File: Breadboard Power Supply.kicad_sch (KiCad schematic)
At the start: 33 parts, among them J1 USB-C Power Only, J10 Conn_01x02_Male, J11 Conn_01x02_Male, J2 Conn_01x02_Male, J3 Conn_01x02_Male, J4 Conn_01x02_Male, J5 Conn_01x02_Male, J6 Conn_01x02_Male, J7 Conn_01x02_Male, J8 Conn_01x02_Male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

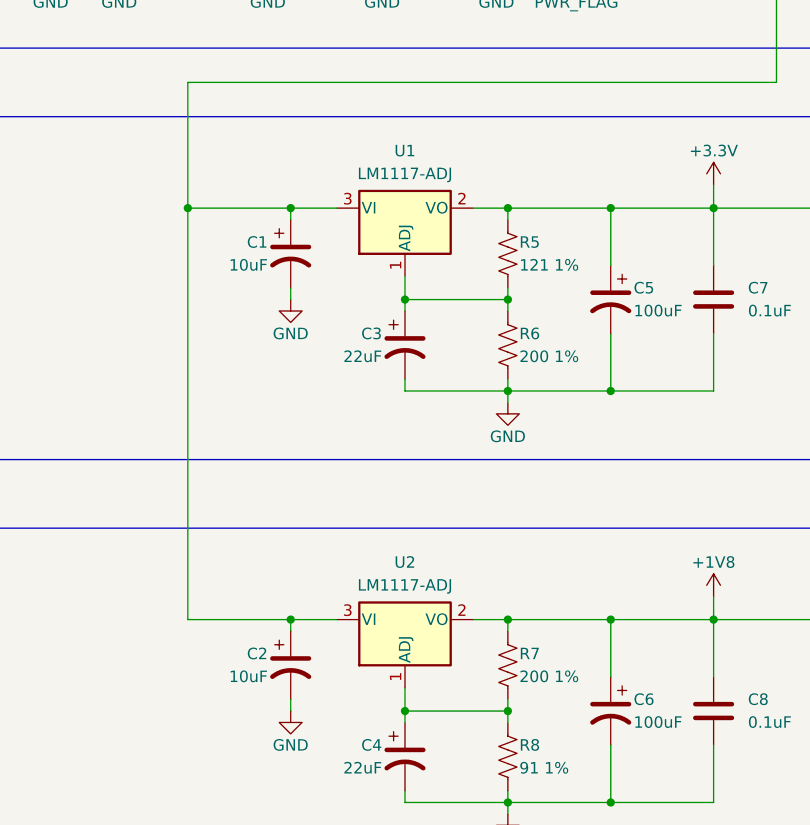
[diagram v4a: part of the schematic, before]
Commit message: Changed LM1117 symbol.
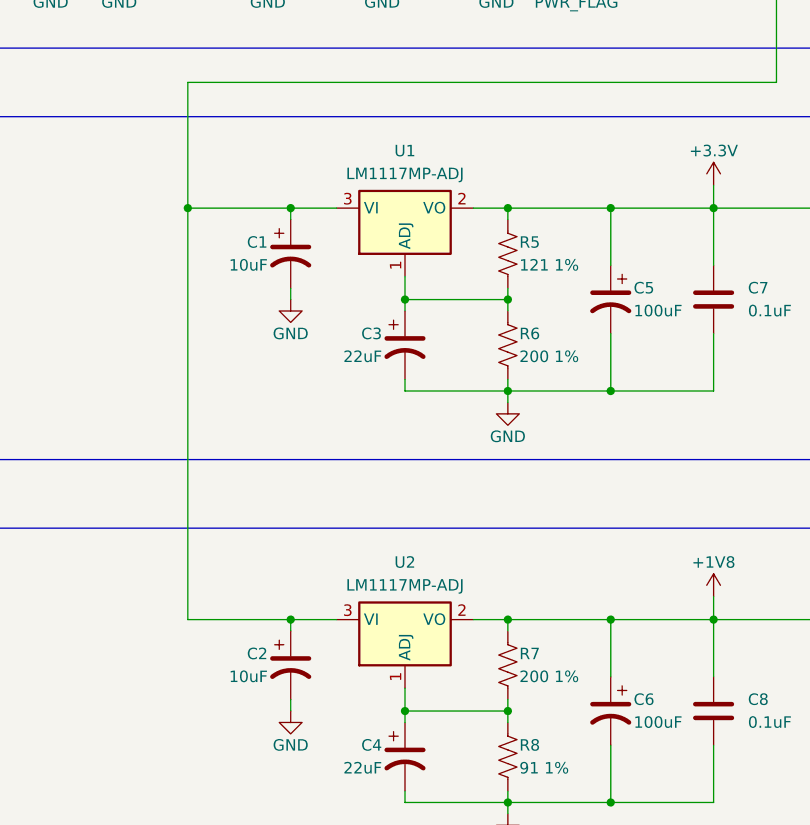
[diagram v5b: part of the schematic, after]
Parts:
- removed U1, U2: LM1117-ADJ, My Breadboard Power Supply Libraries:VREG_LM1117MPX-3.3_NOPB, symbol Regulator_Linear:LM1117-ADJ
- added U1, U2: LM1117MP-ADJ, Package_TO_SOT_SMD:SOT-223-3_TabPin2, symbol Regulator_Linear:LM1117MP-ADJ
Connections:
- net +1V8: now also U2.2 (VO)
- net +3.3V: now also U1.2 (VO)
- net +5V: now also U1.3 (VI), U2.3 (VI)
- net at C4.1, R7.2, R8.1: now also U2.1 (ADJ)
- net at C3.1, R5.2, R6.1: now also U1.1 (ADJ)
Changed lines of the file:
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@@
-    )
-  )
-  (symbol (lib_id "Regulator_Linear:LM1117-ADJ") (at 105.41 97.79 0) (unit 1)
-    (in_bom yes) (on_board yes) (dnp no)
-    (property "Reference" "U1" (at 105.41 91.44 0)
-      (effects (font (size 1.27 1.27)))
-    )
-    (property "Value" "LM1117-ADJ" (at 105.41 93.98 0)
-      (effects (font (size 1.27 1.27)))
-    )
-    (property "Footprint" "My Breadboard Power Supply Libraries:VREG_LM1117MPX-3.3_NOPB" (at 105.41 97.79 0)
-      (effects (font (size 1.27 1.27)) hide)
-    )
-    (property "Datasheet" "http://www.ti.com/lit/ds/symlink/lm1117.pdf" (at 105.41 97.79 0)
-      (effects (font (size 1.27 1.27)) hide)
-    )
-    (pin "1")
-    (pin "2")
-    (pin "3")
-    (instances
-      (project "Breadboard Power Supply"
-        (path "/a474ae98-d5ea-4288-b242-cd0417157b2d"
-          (reference "U1") (unit 1)
-        )
-      )
     )
   )
@@
     )
   )
-  (symbol (lib_id "Regulator_Linear:LM1117-ADJ") (at 105.41 143.51 0) (unit 1)
-    (in_bom yes) (on_board yes) (dnp no)
-    (property "Reference" "U2" (at 105.41 137.16 0)
-      (effects (font (size 1.27 1.27)))
-    )
-    (property "Value" "LM1117-ADJ" (at 105.41 139.7 0)
-      (effects (font (size 1.27 1.27)))
-    )
-    (property "Footprint" "My Breadboard Power Supply Libraries:VREG_LM1117MPX-3.3_NOPB" (at 105.41 143.51 0)
-      (effects (font (size 1.27 1.27)) hide)
-    )
-    (property "Datasheet" "http://www.ti.com/lit/ds/symlink/lm1117.pdf" (at 105.41 143.51 0)
+  (symbol (lib_id "power:GND") (at 210.82 124.46 0) (unit 1)
+    (in_bom yes) (on_board yes) (dnp no)
+    (property "Reference" "#PWR0115" (at 210.82 130.81 0)
+      (effects (font (size 1.27 1.27)) hide)
+    )
+    (property "Value" "GND" (at 210.82 128.27 0)
+      (effects (font (size 1.27 1.27)))
+    )
+    (property "Footprint" "" (at 210.82 124.46 0)
+      (effects (font (size 1.27 1.27)) hide)
+    )
+    (property "Datasheet" "" (at 210.82 124.46 0)
+      (effects (font (size 1.27 1.27)) hide)
+    )
+    (pin "1")
+    (instances
+      (project "Breadboard Power Supply"
+        (path "/a474ae98-d5ea-4288-b242-cd0417157b2d"
+          (reference "#PWR0115") (unit 1)
+        )
+      )
+    )
+  )
+  (symbol (lib_id "Device:R_US") (at 96.52 54.61 90) (unit 1)
+    (in_bom yes) (on_board yes) (dnp no)
+    (property "Reference" "R4" (at 97.79 49.53 90)
+      (effects (font (size 1.27 1.27)) (justify left))
+    )
+    (property "Value" "0 Ohm" (at 100.33 52.07 90)
+      (effects (font (size 1.27 1.27)) (justify left))
+    )
+    (property "Footprint" "Resistor_SMD:R_0603_1608Metric" (at 96.774 53.594 90)
+      (effects (font (size 1.27 1.27)) hide)
+    )
+    (property "Datasheet" "~" (at 96.52 54.61 0)
+      (effects (font (size 1.27 1.27)) hide)
+    )
+    (property "Digi-Key Part Num" "RMCF0805ZT0R00CT-ND" (at 96.52 54.61 90)
+      (effects (font (size 1.27 1.27)) hide)
+    )
+    (pin "1")
+    (pin "2")
+    (instances
+      (project "Breadboard Power Supply"
+        (path "/a474ae98-d5ea-4288-b242-cd0417157b2d"
+          (reference "R4") (unit 1)
+        )
+      )
+    )
+  )
+  (symbol (lib_id "Regulator_Linear:LM1117MP-ADJ") (at 105.41 97.79 0) (unit 1)
+    (in_bom yes) (on_board yes) (dnp no) (fields_autoplaced)
+    (property "Reference" "U1" (at 105.41 91.44 0)
+      (effects (font (size 1.27 1.27)))
+    )
+    (property "Value" "LM1117MP-ADJ" (at 105.41 93.98 0)
+      (effects (font (size 1.27 1.27)))
+    )
+    (property "Footprint" "Package_TO_SOT_SMD:SOT-223-3_TabPin2" (at 105.41 97.79 0)
+      (effects (font (size 1.27 1.27)) hide)
+    )
+    (property "Datasheet" "http://www.ti.com/lit/ds/symlink/lm1117.pdf" (at 105.41 97.79 0)
       (effects (font (size 1.27 1.27)) hide)
     )
@@
       (project "Breadboard Power Supply"
         (path "/a474ae98-d5ea-4288-b242-cd0417157b2d"
-          (reference "U2") (unit 1)
-        )
-      )
-    )
-  )
-  (symbol (lib_id "power:GND") (at 210.82 124.46 0) (unit 1)
-    (in_bom yes) (on_board yes) (dnp no)
-    (property "Reference" "#PWR0115" (at 210.82 130.81 0)
-      (effects (font (size 1.27 1.27)) hide)
-    )
-    (property "Value" "GND" (at 210.82 128.27 0)
-      (effects (font (size 1.27 1.27)))
-    )
-    (property "Footprint" "" (at 210.82 124.46 0)
-      (effects (font (size 1.27 1.27)) hide)
-    )
-    (property "Datasheet" "" (at 210.82 124.46 0)
-      (effects (font (size 1.27 1.27)) hide)
-    )
-    (pin "1")
-    (instances
-      (project "Breadboard Power Supply"
-        (path "/a474ae98-d5ea-4288-b242-cd0417157b2d"
-          (reference "#PWR0115") (unit 1)
-        )
-      )
-    )
-  )
-  (symbol (lib_id "Device:R_US") (at 96.52 54.61 90) (unit 1)
-    (in_bom yes) (on_board yes) (dnp no)
-    (property "Reference" "R4" (at 97.79 49.53 90)
-      (effects (font (size 1.27 1.27)) (justify left))
-    )
-    (property "Value" "0 Ohm" (at 100.33 52.07 90)
-      (effects (font (size 1.27 1.27)) (justify left))
-    )
-    (property "Footprint" "Resistor_SMD:R_0603_1608Metric" (at 96.774 53.594 90)
-      (effects (font (size 1.27 1.27)) hide)
-    )
-    (property "Datasheet" "~" (at 96.52 54.61 0)
-      (effects (font (size 1.27 1.27)) hide)
-    )
-    (property "Digi-Key Part Num" "RMCF0805ZT0R00CT-ND" (at 96.52 54.61 90)
-      (effects (font (size 1.27 1.27)) hide)
-    )
-    (pin "1")
-    (pin "2")
-    (instances
-      (project "Breadboard Power Supply"
-        (path "/a474ae98-d5ea-4288-b242-cd0417157b2d"
-          (reference "R4") (unit 1)
+          (reference "U1") (unit 1)
         )
       )
@@
         )
       )
+    )
+  )
+  (symbol (lib_id "Regulator_Linear:LM1117MP-ADJ") (at 105.41 143.51 0) (unit 1)
+    (in_bom yes) (on_board yes) (dnp no) (fields_autoplaced)
+    (property "Reference" "U2" (at 105.41 137.16 0)
+      (effects (font (size 1.27 1.27)))
+    )
+    (property "Value" "LM1117MP-ADJ" (at 105.41 139.7 0)
+      (effects (font (size 1.27 1.27)))
+    )
+    (property "Footprint" "Package_TO_SOT_SMD:SOT-223-3_TabPin2" (at 105.41 143.51 0)
+      (effects (font (size 1.27 1.27)) hide)
+    )
+    (property "Datasheet" "http://www.ti.com/lit/ds/symlink/lm1117.pdf" (at 105.41 143.51 0)
+      (effects (font (size 1.27 1.27)) hide)
+    )
+    (pin "1")
+    (pin "2")
+    (pin "3")
+    (instances
+      (project "Breadboard Power Supply"
+        (path "/a474ae98-d5ea-4288-b242-cd0417157b2d"
+          (reference "U2") (unit 1)
+        )
+      )

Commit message: Update.
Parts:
- removed VR1: LM1117MPX-3.3/NOPB, VREG_LM1117MPX-3.3/NOPB, symbol LM1117MPX-3.3_NOPB:LM1117MPX-3.3/NOPB
- added J12: 217175-0001, 2171750001, symbol USB-C Surface Mount:217175-0001
- J1: footprint USB4085-GF-A_REVA4:GCT_USB4085-GF-A_REVA4 -> USC-C Surface Mount:2171750001
- renumbered U2 to U1, U1 to U2
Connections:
- net GND: no longer J10.1 (Pin_1), J10.2 (Pin_2), J11.1 (Pin_1), J11.2 (Pin_2)
- no-connect marks 0 -> 4
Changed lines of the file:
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@@
   (junction (at 90.17 59.69) (diameter 0) (color 0 0 0 0)
   )
-  (junction (at 198.12 152.4) (diameter 0) (color 0 0 0 0)
-  )
-  (junction (at 187.96 152.4) (diameter 0) (color 0 0 0 0)
-  )
   (junction (at 81.28 97.79) (diameter 0) (color 0 0 0 0)
   )
@@
   (junction (at 139.7 143.51) (diameter 0) (color 0 0 0 0)
   )
+  (no_connect (at 199.39 151.13))
+  (no_connect (at 186.69 151.13))
+  (no_connect (at 196.85 151.13))
+  (no_connect (at 189.23 151.13))
   (wire (pts (xy 146.685 83.82) (xy 81.28 83.82))
     (stroke (width 0) (type default))
@@
     (stroke (width 0) (type default))
   )
-  (wire (pts (xy 187.96 152.4) (xy 187.96 153.67))
-    (stroke (width 0) (type default))
-  )
   (wire (pts (xy 139.7 140.97) (xy 139.7 143.51))
     (stroke (width 0) (type default))
@@
     (stroke (width 0) (type default))
   )
-  (wire (pts (xy 187.96 152.4) (xy 189.23 152.4))
-    (stroke (width 0) (type default))
-  )
   (wire (pts (xy 90.17 59.69) (xy 88.9 59.69))
     (stroke (width 0) (type default))
@@
     (stroke (width 0) (type default))
   )
-  (wire (pts (xy 198.12 152.4) (xy 198.12 153.67))
-    (stroke (width 0) (type default))
-  )
   (wire (pts (xy 115.57 68.58) (xy 124.46 68.58))
     (stroke (width 0) (type default))
@@
     (stroke (width 0) (type default))
   )
-  (wire (pts (xy 196.85 152.4) (xy 198.12 152.4))
-    (stroke (width 0) (type default))
-  )
   (wire (pts (xy 66.04 69.85) (xy 66.04 71.12))
     (stroke (width 0) (type default))
@@
     (stroke (width 0) (type default))
   )
-  (wire (pts (xy 196.85 151.13) (xy 196.85 152.4))
-    (stroke (width 0) (type default))
-  )
-  (wire (pts (xy 199.39 151.13) (xy 199.39 152.4))
-    (stroke (width 0) (type default))
-  )
   (wire (pts (xy 116.84 107.95) (xy 116.84 109.22))
     (stroke (width 0) (type default))
@@
     (stroke (width 0) (type default))
   )
-  (wire (pts (xy 186.69 152.4) (xy 187.96 152.4))
-    (stroke (width 0) (type default))
-  )
   (wire (pts (xy 105.41 151.13) (xy 105.41 153.67))
     (stroke (width 0) (type default))
@@
     (stroke (width 0) (type default))
   )
-  (wire (pts (xy 189.23 151.13) (xy 189.23 152.4))
-    (stroke (width 0) (type default))
-  )
   (wire (pts (xy 146.685 44.45) (xy 146.685 83.82))
     (stroke (width 0) (type default))
@@
     (stroke (width 0) (type default))
   )
-  (wire (pts (xy 198.12 152.4) (xy 199.39 152.4))
-    (stroke (width 0) (type default))
-  )
   (wire (pts (xy 171.45 58.42) (xy 180.34 58.42))
     (stroke (width 0) (type default))
@@
   )
   (wire (pts (xy 88.9 44.45) (xy 115.57 44.45))
-    (stroke (width 0) (type default))
-  )
-  (wire (pts (xy 186.69 151.13) (xy 186.69 152.4))
     (stroke (width 0) (type default))
   )
@@
         (path "/a474ae98-d5ea-4288-b242-cd0417157b2d"
           (reference "#PWR0109") (unit 1)
-        )
-      )
-    )
-  )
-  (symbol (lib_id "power:GND") (at 187.96 153.67 0) (unit 1)
-    (in_bom yes) (on_board yes) (dnp no)
-    (property "Reference" "#PWR01" (at 187.96 160.02 0)
-      (effects (font (size 1.27 1.27)) hide)
-    )
-    (property "Value" "GND" (at 187.96 157.48 0)
-      (effects (font (size 1.27 1.27)))
-    )
-    (property "Footprint" "" (at 187.96 153.67 0)
-      (effects (font (size 1.27 1.27)) hide)
-    )
-    (property "Datasheet" "" (at 187.96 153.67 0)
-      (effects (font (size 1.27 1.27)) hide)
-    )
-    (pin "1")
-    (instances
-      (project "Breadboard Power Supply"
-        (path "/a474ae98-d5ea-4288-b242-cd0417157b2d"
-          (reference "#PWR01") (unit 1)
         )
       )
@@
     )
   )
-  (symbol (lib_id "LM1117MPX-3.3_NOPB:LM1117MPX-3.3{slash}NOPB") (at 204.851 29.591 0) (unit 1)
-    (in_bom yes) (on_board yes) (dnp no) (fields_autoplaced)
-    (property "Reference" "VR1" (at 204.851 20.32 0)
-      (effects (font (size 1.27 1.27)))
-    )
-    (property "Value" "LM1117MPX-3.3/NOPB" (at 204.851 22.86 0)
-      (effects (font (size 1.27 1.27)))
-    )
-    (property "Footprint" "VREG_LM1117MPX-3.3/NOPB" (at 204.851 29.591 0)
-      (effects (font (size 1.27 1.27)) (justify bottom) hide)
-    )
-    (property "Datasheet" "" (at 204.851 29.591 0)
-      (effects (font (size 1.27 1.27)) hide)
-    )
-    (property "MAXIMUM_PACKAGE_HEIGHT" "1.80 mm" (at 204.851 29.591 0)
-      (effects (font (size 1.27 1.27)) (justify bottom) hide)
-    )
-    (property "STANDARD" "Manufacturer Recommendation" (at 204.851 29.591 0)
-      (effects (font (size 1.27 1.27)) (justify bottom) hide)
-    )
-    (property "PARTREV" "O" (at 204.851 29.591 0)
-      (effects (font (size 1.27 1.27)) (justify bottom) hide)
-    )
-    (property "MANUFACTURER" "Texas Instruments" (at 204.851 29.591 0)
-      (effects (font (size 1.27 1.27)) (justify bottom) hide)
-    )
-    (pin "1")
-    (pin "2")
-    (pin "3")
-    (pin "4")
-    (instances
-      (project "Breadboard Power Supply"
-        (path "/a474ae98-d5ea-4288-b242-cd0417157b2d"
-          (reference "VR1") (unit 1)
-        )
-      )
-    )
-  )
   (symbol (lib_id "power:GND") (at 115.57 71.12 0) (unit 1)
     (in_bom yes) (on_board yes) (dnp no)
@@
     )
   )
+  (symbol (lib_id "USB-C Surface Mount:217175-0001") (at 26.797 48.641 0) (unit 1)
+    (in_bom yes) (on_board yes) (dnp no) (fields_autoplaced)
+    (property "Reference" "J12" (at 43.307 41.656 0)
+      (effects (font (size 1.27 1.27)))
+    )
+    (property "Value" "217175-0001" (at 43.307 44.196 0)
+      (effects (font (size 1.27 1.27)))
+    )
+    (property "Footprint" "2171750001" (at 56.007 46.101 0)
+      (effects (font (size 1.27 1.27)) (justify left) hide)
+    )
+    (property "Datasheet" "https://www.molex.com/pdm_docs/sd/2171750001_sd.pdf" (at 56.007 48.641 0)
+      (effects (font (size 1.27 1.27)) (justify left) hide)
+    )
+    (property "Description" "Connector USB Type C Female 6Positions 0.5mm Right Angle SMT Embossed T/R - Tape and Reel" (at 56.007 51.181 0)
+      (effects (font (size 1.27 1.27)) (justify left) hide)
+    )
+    (property "Height" "3.46" (at 56.007 53.721 0)
+      (effects (font (size 1.27 1.27)) (justify left) hide)
+    )
+    (property "Manufacturer_Name" "Molex" (at 56.007 56.261 0)
+      (effects (font (size 1.27 1.27)) (justify left) hide)
+    )
+    (property "Manufacturer_Part_Number" "217175-0001" (at 56.007 58.801 0)
+      (effects (font (size 1.27 1.27)) (justify left) hide)
+    )
+    (property "Mouser Part Number" "538-217175-0001" (at 56.007 61.341 0)
+      (effects (font (size 1.27 1.27)) (justify left) hide)
+    )
+    (property "Mouser Price/Stock" "https://www.mouser.co.uk/ProductDetail/Molex/217175-0001?qs=DRkmTr78QARWJMiqNnldSg%3D%3D" (at 56.007 63.881 0)
+      (effects (font (size 1.27 1.27)) (justify left) hide)
+    )
+    (property "Arrow Part Number" "" (at 56.007 66.421 0)
+      (effects (font (size 1.27 1.27)) (justify left) hide)
+    )
+    (property "Arrow Price/Stock" "" (at 56.007 68.961 0)
+      (effects (font (size 1.27 1.27)) (justify left) hide)
+    )
+    (property "Mouser Testing Part Number" "" (at 56.007 71.501 0)
+      (effects (font (size 1.27 1.27)) (justify left) hide)
+    )
+    (property "Mouser Testing Price/Stock" "" (at 56.007 74.041 0)
+      (effects (font (size 1.27 1.27)) (justify left) hide)
+    )
+    (pin "A12")
+    (pin "A5")
+    (pin "A9")
+    (pin "B12")
+    (pin "B5")
+    (pin "B9")
+    (pin "MH1")
+    (pin "MH2")
+    (pin "MH3")
+    (pin "MH4")
+    (instances
+      (project "Breadboard Power Supply"
+        (path "/a474ae98-d5ea-4288-b242-cd0417157b2d"
+          (reference "J12") (unit 1)
+        )
+      )
+    )
+  )
   (symbol (lib_id "power:GND") (at 73.66 71.12 0) (unit 1)
     (in_bom yes) (on_board yes) (dnp no)
@@
     )
   )
-  (symbol (lib_id "power:GND") (at 198.12 153.67 0) (unit 1)
-    (in_bom yes) (on_board yes) (dnp no)
-    (property "Reference" "#PWR02" (at 198.12 160.02 0)
-      (effects (font (size 1.27 1.27)) hide)
-    )
-    (property "Value" "GND" (at 198.12 157.48 0)
-      (effects (font (size 1.27 1.27)))
-    )
-    (property "Footprint" "" (at 198.12 153.67 0)
-      (effects (font (size 1.27 1.27)) hide)
-    )
-    (property "Datasheet" "" (at 198.12 153.67 0)
-      (effects (font (size 1.27 1.27)) hide)
-    )
-    (pin "1")
-    (instances
-      (project "Breadboard Power Supply"
-        (path "/a474ae98-d5ea-4288-b242-cd0417157b2d"
-          (reference "#PWR02") (unit 1)
-        )
-      )
-    )
-  )
   (symbol (lib_id "power:GND") (at 210.82 124.46 0) (unit 1)
     (in_bom yes) (on_board yes) (dnp no)
@@
   (symbol (lib_id "Regulator_Linear:LM1117MP-ADJ") (at 105.41 97.79 0) (unit 1)
     (in_bom yes) (on_board yes) (dnp no) (fields_autoplaced)
-    (property "Reference" "U1" (at 105.41 91.44 0)
+    (property "Reference" "U2" (at 105.41 91.44 0)
       (effects (font (size 1.27 1.27)))
     )
@@
       (project "Breadboard Power Supply"
         (path "/a474ae98-d5ea-4288-b242-cd0417157b2d"
-          (reference "U1") (unit 1)
+          (reference "U2") (unit 1)
         )
       )
@@
   (symbol (lib_id "Regulator_Linear:LM1117MP-ADJ") (at 105.41 143.51 0) (unit 1)
     (in_bom yes) (on_board yes) (dnp no) (fields_autoplaced)
-    (property "Reference" "U2" (at 105.41 137.16 0)
+    (property "Reference" "U1" (at 105.41 137.16 0)
       (effects (font (size 1.27 1.27)))
     )
@@
       (project "Breadboard Power Supply"
         (path "/a474ae98-d5ea-4288-b242-cd0417157b2d"
-          (reference "U2") (unit 1)
+          (reference "U1") (unit 1)
         )
       )
@@
       (effects (font (size 1.27 1.27)))
     )
-    (property "Footprint" "USB4085-GF-A_REVA4:GCT_USB4085-GF-A_REVA4" (at 77.47 49.53 0)
-      (effects (font (size 1.27 1.27)) hide)
-    )
+    (property "Footprint" "USC-C Surface Mount:2171750001" (at 77.47 49.53 0)
+      (effects (font (size 1.27 1.27)) hide)
+    )
